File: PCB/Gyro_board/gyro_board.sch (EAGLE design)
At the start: 5 parts, among them P1 WISP_HEADER, U1 BGM250

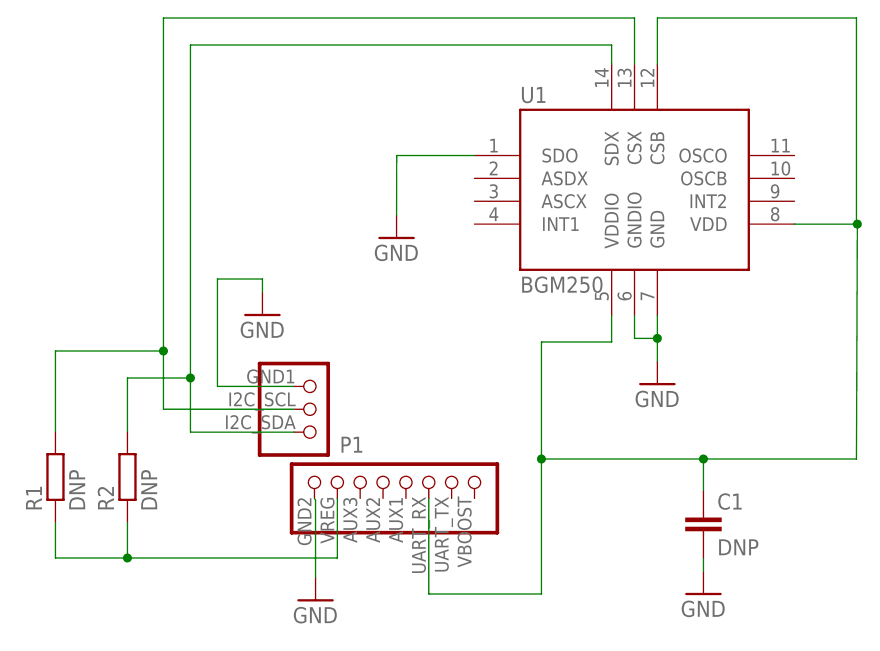
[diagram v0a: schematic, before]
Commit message: Fix component name typo
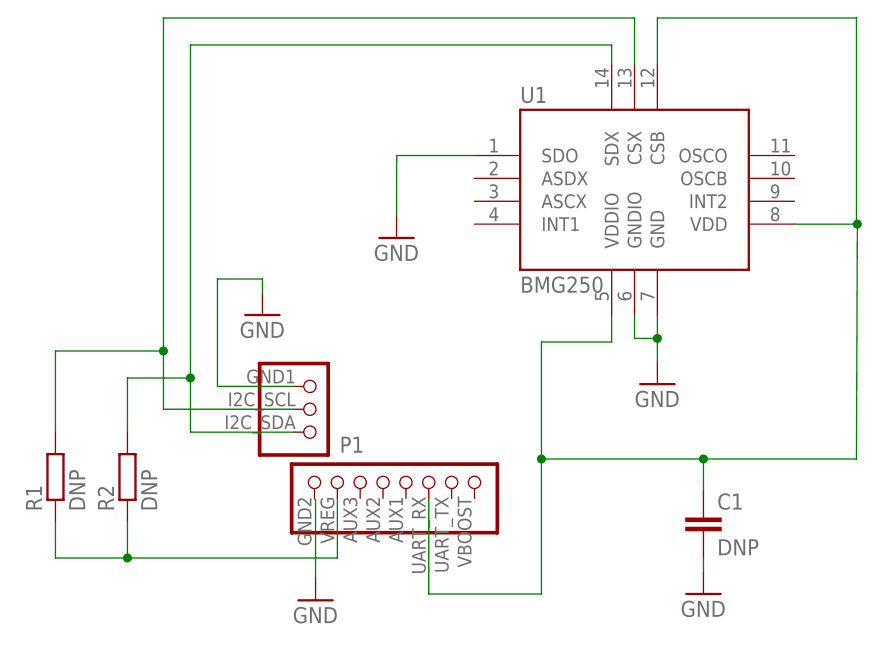
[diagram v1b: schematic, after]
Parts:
- U1: value BGM250 -> BMG250
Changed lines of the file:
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@@
 <parts>
 <part name="P1" library="robot_pcb2" deviceset="WISP_HEADER" device=""/>
-<part name="U1" library="robot_pcb2" deviceset="BGM250" device=""/>
+<part name="U1" library="robot_pcb2" deviceset="BGM250" device="" value="BMG250"/>
 <part name="GND1" library="Wisp5_Harvester_Motor-driver" deviceset="GND" device=""/>
 <part name="GND2" library="Wisp5_Harvester_Motor-driver" deviceset="GND" device=""/>
